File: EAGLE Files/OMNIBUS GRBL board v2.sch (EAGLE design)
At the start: 61 parts, among them K1 691131710002, K2 691131710003, K3 691131710003, K4 691131710003, U1 LTV-847S, U2 L7805ACD2T-TR, U3 LM358M/NOPB, U4 LTV-847S, U5 PC817X3NSZ1B, U6 ULN2003AD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

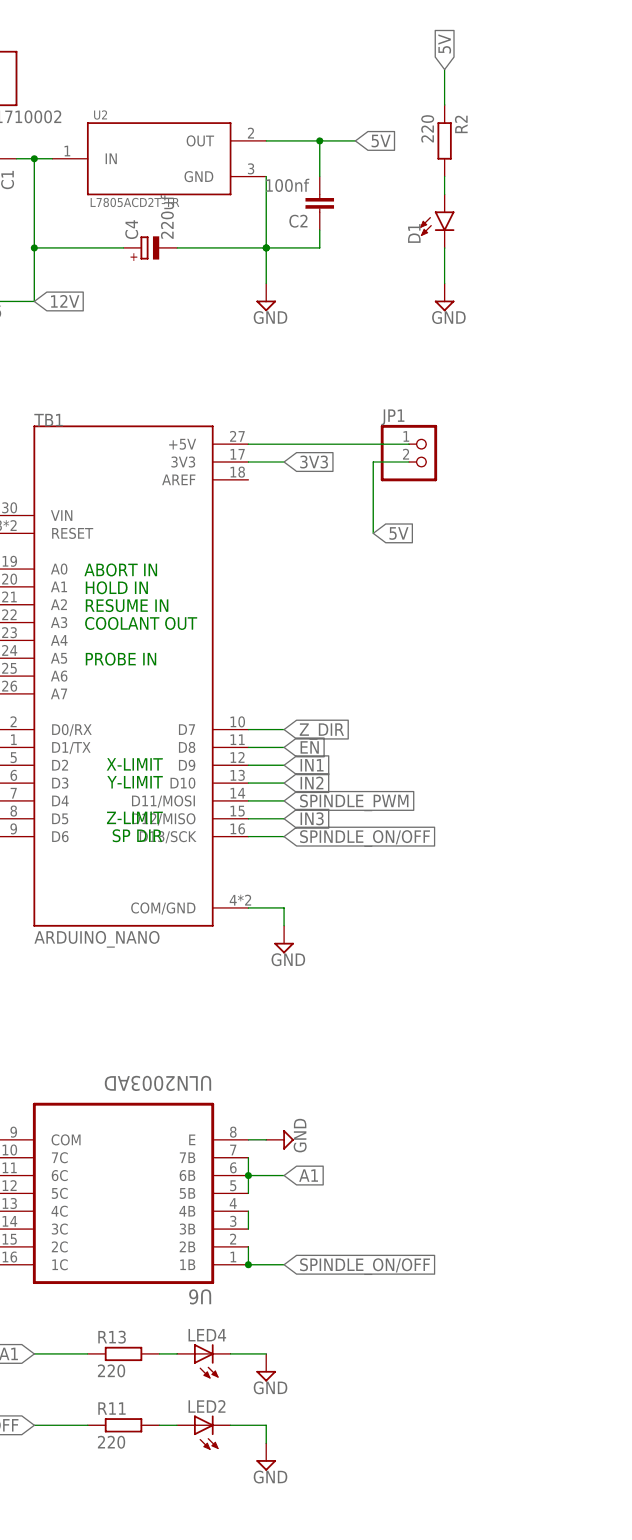
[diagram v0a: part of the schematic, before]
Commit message: PCB Bugfixes and polishing
• DRV Shield had an routing error (laser indicator LED) also R3 had a wrong value
• New Footprint for the 0.33uF Caps
• Silkscreen polishing
• almost all LEDs are 0805 package now
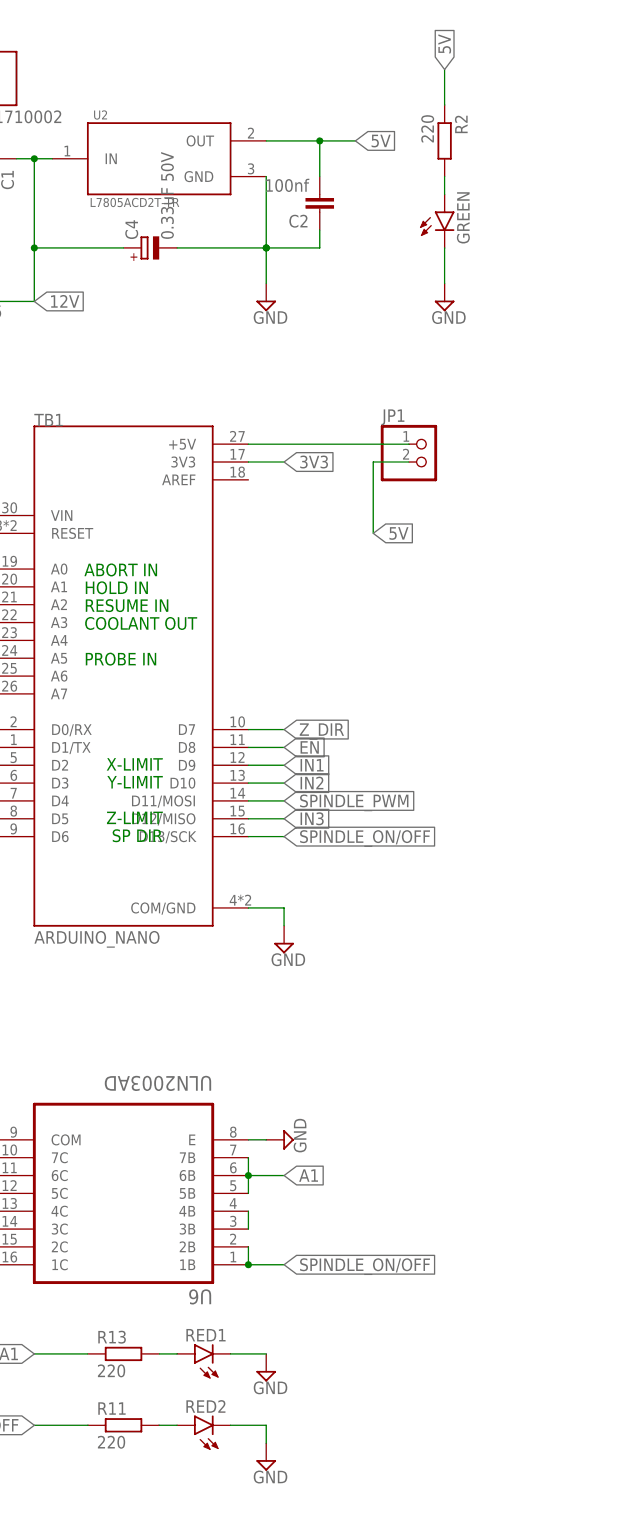
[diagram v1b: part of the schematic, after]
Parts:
- removed D1: (no value), SparkFun-LED:LED1206
- removed LED2, LED4: (no value), eagle-ltspice:LED_ESML0603
- added GREEN, RED1, RED2: (no value), led:LEDCHIPLED_0805
- C4: value 220uf -> 0.33uF 50V; device rcl:CPOL-EUE5-6 -> rcl:CPOL-EUE2-5
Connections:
- net GND: now also GREEN.C, RED1.C, RED2.C; no longer D1.C, LED2.C, LED4.C
- net N$1: now also GREEN.A; no longer D1.A
- net N$11: now also RED2.A; no longer LED2.A
- net N$12: now also RED1.A; no longer LED4.A

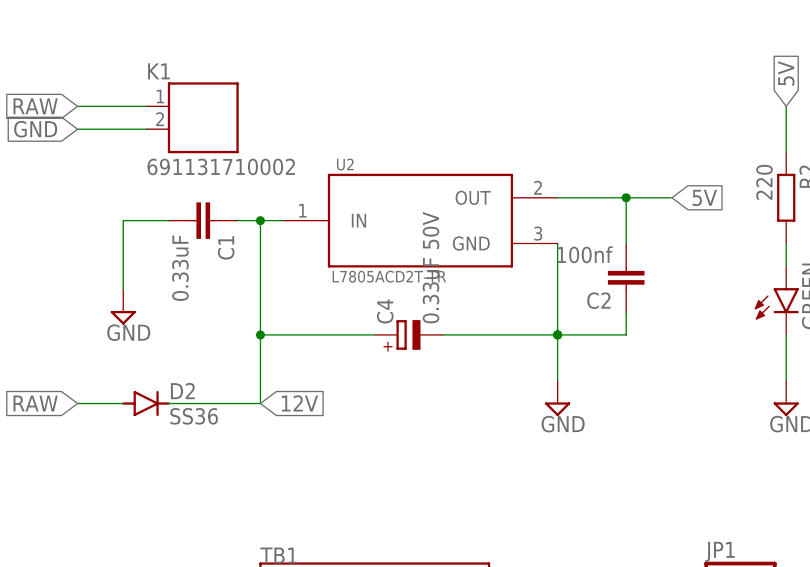
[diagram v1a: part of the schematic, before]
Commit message: Changed voltage regulators
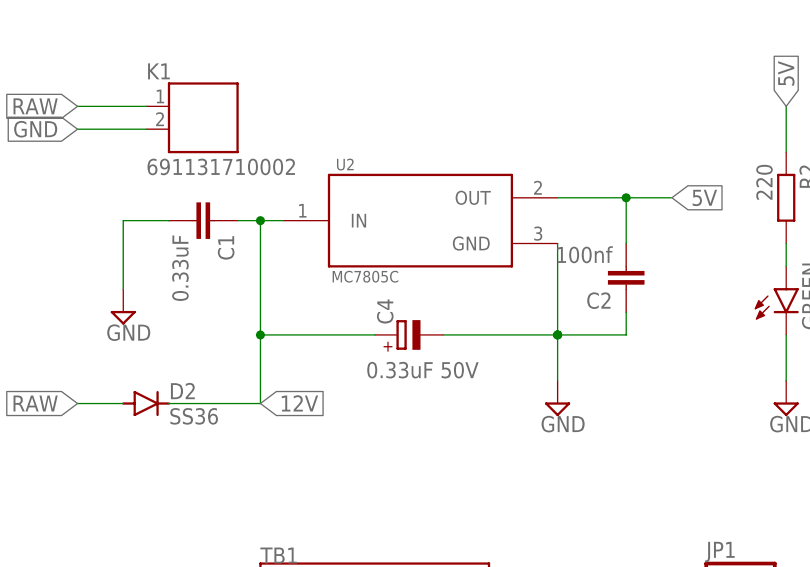
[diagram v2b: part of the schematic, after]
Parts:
- U2: value L7805ACD2T-TR -> MC7805C
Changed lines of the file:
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@@
 <grid distance="0.1" unitdist="inch" unit="inch" style="lines" multiple="1" display="no" altdistance="0.01" altunitdist="inch" altunit="inch"/>
 <layers>
-<layer number="1" name="Top" color="4" fill="1" visible="yes" active="no"/>
-<layer number="2" name="Route2" color="16" fill="1" visible="yes" active="no"/>
-<layer number="3" name="Route3" color="17" fill="1" visible="yes" active="no"/>
-<layer number="4" name="Route4" color="18" fill="1" visible="yes" active="no"/>
-<layer number="5" name="Route5" color="19" fill="1" visible="yes" active="no"/>
-<layer number="6" name="Route6" color="25" fill="1" visible="yes" active="no"/>
-<layer number="7" name="Route7" color="26" fill="1" visible="yes" active="no"/>
-<layer number="8" name="Route8" color="27" fill="1" visible="yes" active="no"/>
-<layer number="9" name="Route9" color="28" fill="1" visible="yes" active="no"/>
-<layer number="10" name="Route10" color="29" fill="1" visible="yes" active="no"/>
-<layer number="11" name="Route11" color="30" fill="1" visible="yes" active="no"/>
-<layer number="12" name="Route12" color="20" fill="1" visible="yes" active="no"/>
-<layer number="13" name="Route13" color="21" fill="1" visible="yes" active="no"/>
-<layer number="14" name="Route14" color="22" fill="1" visible="yes" active="no"/>
-<layer number="15" name="Route15" color="23" fill="1" visible="yes" active="no"/>
-<layer number="16" name="Bottom" color="1" fill="1" visible="yes" active="no"/>
-<layer number="17" name="Pads" color="2" fill="1" visible="yes" active="no"/>
-<layer number="18" name="Vias" color="2" fill="1" visible="yes" active="no"/>
-<layer number="19" name="Unrouted" color="6" fill="1" visible="yes" active="no"/>
-<layer number="20" name="Dimension" color="24" fill="1" visible="yes" active="no"/>
-<layer number="21" name="tPlace" color="7" fill="1" visible="yes" active="no"/>
-<layer number="22" name="bPlace" color="7" fill="1" visible="yes" active="no"/>
-<layer number="23" name="tOrigins" color="15" fill="1" visible="yes" active="no"/>
-<layer number="24" name="bOrigins" color="15" fill="1" visible="yes" active="no"/>
-<layer number="25" name="tNames" color="7" fill="1" visible="yes" active="no"/>
-<layer number="26" name="bNames" color="7" fill="1" visible="yes" active="no"/>
-<layer number="27" name="tValues" color="7" fill="1" visible="yes" active="no"/>
-<layer number="28" name="bValues" color="7" fill="1" visible="yes" active="no"/>
+<layer number="1" name="Top" color="4" fill="1" visible="no" active="no"/>
+<layer number="2" name="Route2" color="16" fill="1" visible="no" active="no"/>
+<layer number="3" name="Route3" color="17" fill="1" visible="no" active="no"/>
+<layer number="4" name="Route4" color="18" fill="1" visible="no" active="no"/>
+<layer number="5" name="Route5" color="19" fill="1" visible="no" active="no"/>
+<layer number="6" name="Route6" color="25" fill="1" visible="no" active="no"/>
+<layer number="7" name="Route7" color="26" fill="1" visible="no" active="no"/>
+<layer number="8" name="Route8" color="27" fill="1" visible="no" active="no"/>
+<layer number="9" name="Route9" color="28" fill="1" visible="no" active="no"/>
+<layer number="10" name="Route10" color="29" fill="1" visible="no" active="no"/>
+<layer number="11" name="Route11" color="30" fill="1" visible="no" active="no"/>
+<layer number="12" name="Route12" color="20" fill="1" visible="no" active="no"/>
+<layer number="13" name="Route13" color="21" fill="1" visible="no" active="no"/>
+<layer number="14" name="Route14" color="22" fill="1" visible="no" active="no"/>
+<layer number="15" name="Route15" color="23" fill="1" visible="no" active="no"/>
+<layer number="16" name="Bottom" color="1" fill="1" visible="no" active="no"/>
+<layer number="17" name="Pads" color="2" fill="1" visible="no" active="no"/>
+<layer number="18" name="Vias" color="2" fill="1" visible="no" active="no"/>
+<layer number="19" name="Unrouted" color="6" fill="1" visible="no" active="no"/>
+<layer number="20" name="Dimension" color="24" fill="1" visible="no" active="no"/>
+<layer number="21" name="tPlace" color="7" fill="1" visible="no" active="no"/>
+<layer number="22" name="bPlace" color="7" fill="1" visible="no" active="no"/>
+<layer number="23" name="tOrigins" color="15" fill="1" visible="no" active="no"/>
+<layer number="24" name="bOrigins" color="15" fill="1" visible="no" active="no"/>
+<layer number="25" name="tNames" color="7" fill="1" visible="no" active="no"/>
+<layer number="26" name="bNames" color="7" fill="1" visible="no" active="no"/>
+<layer number="27" name="tValues" color="7" fill="1" visible="no" active="no"/>
+<layer number="28" name="bValues" color="7" fill="1" visible="no" active="no"/>
 <layer number="29" name="tStop" color="7" fill="3" visible="no" active="no"/>
 <layer number="30" name="bStop" color="7" fill="6" visible="no" active="no"/>
@@
 <layer number="35" name="tGlue" color="7" fill="4" visible="no" active="no"/>
 <layer number="36" name="bGlue" color="7" fill="5" visible="no" active="no"/>
-<layer number="37" name="tTest" color="7" fill="1" visible="yes" active="no"/>
-<layer number="38" name="bTest" color="7" fill="1" visible="yes" active="no"/>
+<layer number="37" name="tTest" color="7" fill="1" visible="no" active="no"/>
+<layer number="38" name="bTest" color="7" fill="1" visible="no" active="no"/>
 <layer number="39" name="tKeepout" color="4" fill="11" visible="no" active="no"/>
 <layer number="40" name="bKeepout" color="1" fill="11" visible="no" active="no"/>
@@
 <layer number="44" name="Drills" color="7" fill="1" visible="no" active="no"/>
 <layer number="45" name="Holes" color="7" fill="1" visible="no" active="no"/>
-<layer number="46" name="Milling" color="3" fill="1" visible="yes" active="no"/>
-<layer number="47" name="Measures" color="7" fill="1" visible="yes" active="no"/>
-<layer number="48" name="Document" color="7" fill="1" visible="yes" active="no"/>
-<layer number="49" name="Reference" color="7" fill="1" visible="yes" active="no"/>
-<layer number="50" name="dxf" color="7" fill="1" visible="yes" active="no"/>
-<layer number="51" name="tDocu" color="7" fill="1" visible="yes" active="no"/>
-<layer number="52" name="bDocu" color="7" fill="1" visible="yes" active="no"/>
-<layer number="53" name="tGND_GNDA" color="7" fill="1" visible="yes" active="no"/>
-<layer number="54" name="bGND_GNDA" color="7" fill="1" visible="yes" active="no"/>
-<layer number="56" name="wert" color="7" fill="1" visible="yes" active="no"/>
-<layer number="57" name="tCAD" color="7" fill="1" visible="yes" active="no"/>
-<layer number="59" name="tCarbon" color="7" fill="1" visible="yes" active="no"/>
-<layer number="60" name="bCarbon" color="7" fill="1" visible="yes" active="no"/>
+<layer number="46" name="Milling" color="3" fill="1" visible="no" active="no"/>
+<layer number="47" name="Measures" color="7" fill="1" visible="no" active="no"/>
+<layer number="48" name="Document" color="7" fill="1" visible="no" active="no"/>
+<layer number="49" name="Reference" color="7" fill="1" visible="no" active="no"/>
+<layer number="50" name="dxf" color="7" fill="1" visible="no" active="no"/>
+<layer number="51" name="tDocu" color="7" fill="1" visible="no" active="no"/>
+<layer number="52" name="bDocu" color="7" fill="1" visible="no" active="no"/>
+<layer number="53" name="tGND_GNDA" color="7" fill="1" visible="no" active="no"/>
+<layer number="54" name="bGND_GNDA" color="7" fill="1" visible="no" active="no"/>
+<layer number="56" name="wert" color="7" fill="1" visible="no" active="no"/>
+<layer number="57" name="tCAD" color="7" fill="1" visible="no" active="no"/>
+<layer number="59" name="tCarbon" color="7" fill="1" visible="no" active="no"/>
+<layer number="60" name="bCarbon" color="7" fill="1" visible="no" active="no"/>
 <layer number="88" name="SimResults" color="9" fill="1" visible="yes" active="yes"/>
 <layer number="89" name="SimProbes" color="9" fill="1" visible="yes" active="yes"/>
@@
 <part name="K1" library="Wurth_Terminal_Blocks_Connectors_rev15d" deviceset="691131710002" device=""/>
 <part name="U1" library="LTV-847S" deviceset="LTV-847S" device=""/>
-<part name="U2" library="L7805ACD2T-TR" deviceset="L7805ACD2T-TR" device=""/>
+<part name="U2" library="L7805ACD2T-TR" deviceset="L7805ACD2T-TR" device="" value="MC7805C"/>
 <part name="U3" library="LM358M_NOPB" deviceset="LM358M/NOPB" device=""/>
 <part name="VR1" library="3296W-1-502" deviceset="3296W-1-502" device="" value="10k"/>
@@
 <instance part="C4" gate="G$1" x="33.02" y="175.26" smashed="yes" rot="R90">
 <attribute name="NAME" x="32.5374" y="176.403" size="1.778" layer="95" rot="R90"/>
-<attribute name="VALUE" x="37.6174" y="176.403" size="1.778" layer="96" rot="R90"/>
+<attribute name="VALUE" x="42.037" y="172.2374" size="1.778" layer="96" rot="R180"/>
 </instance>
 <instance part="RESET" gate="-1" x="170.18" y="43.18" smashed="yes" rot="R90">

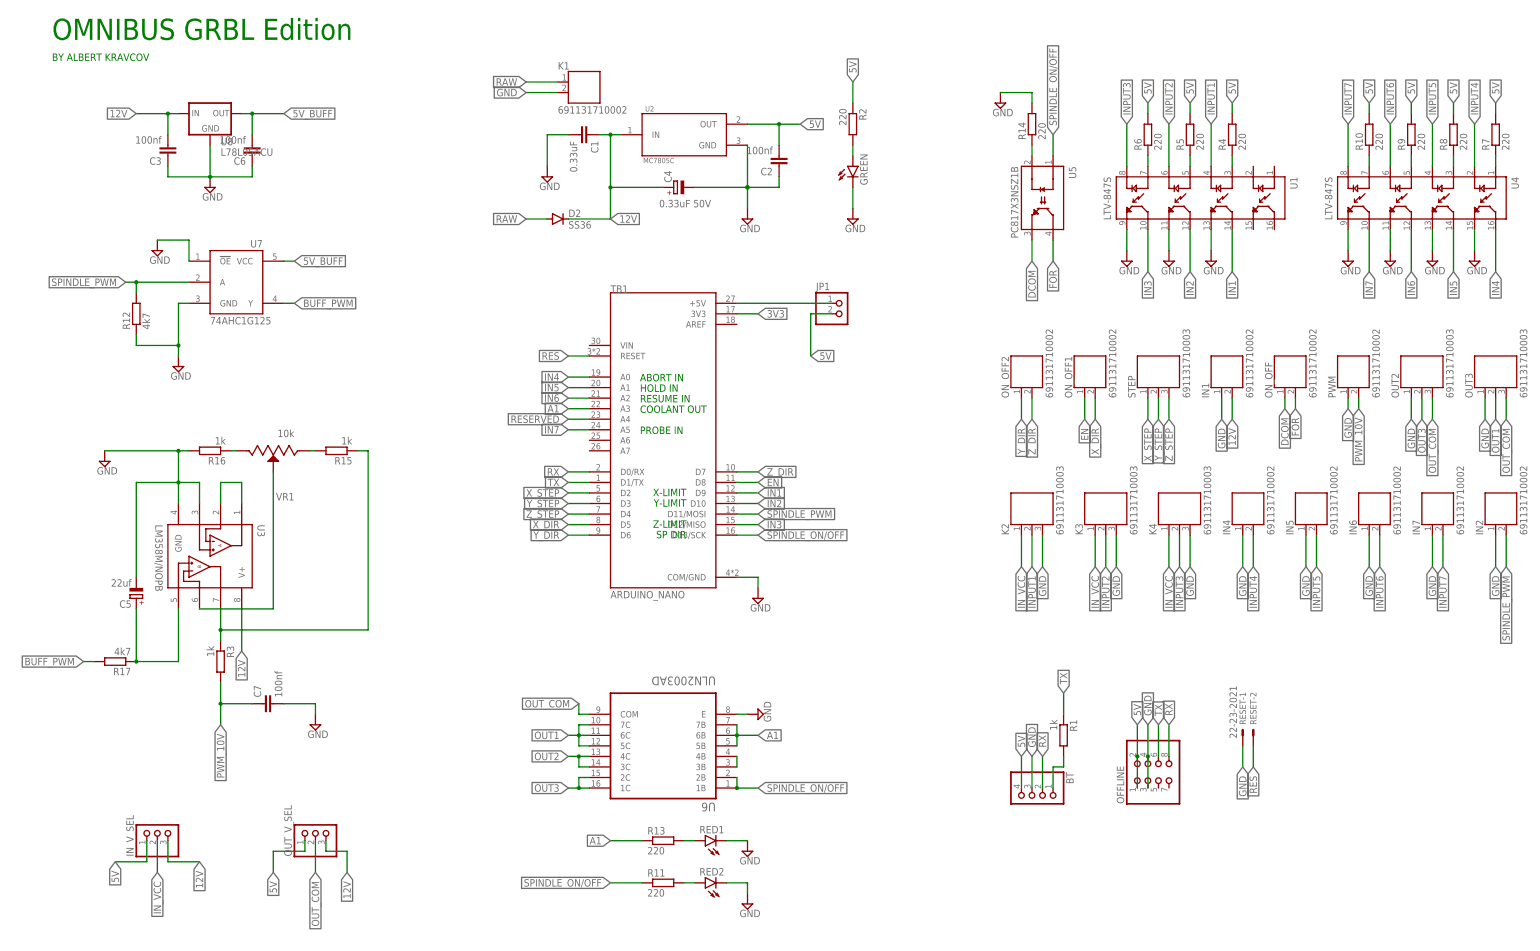
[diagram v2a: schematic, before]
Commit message: clean up
also added BOM
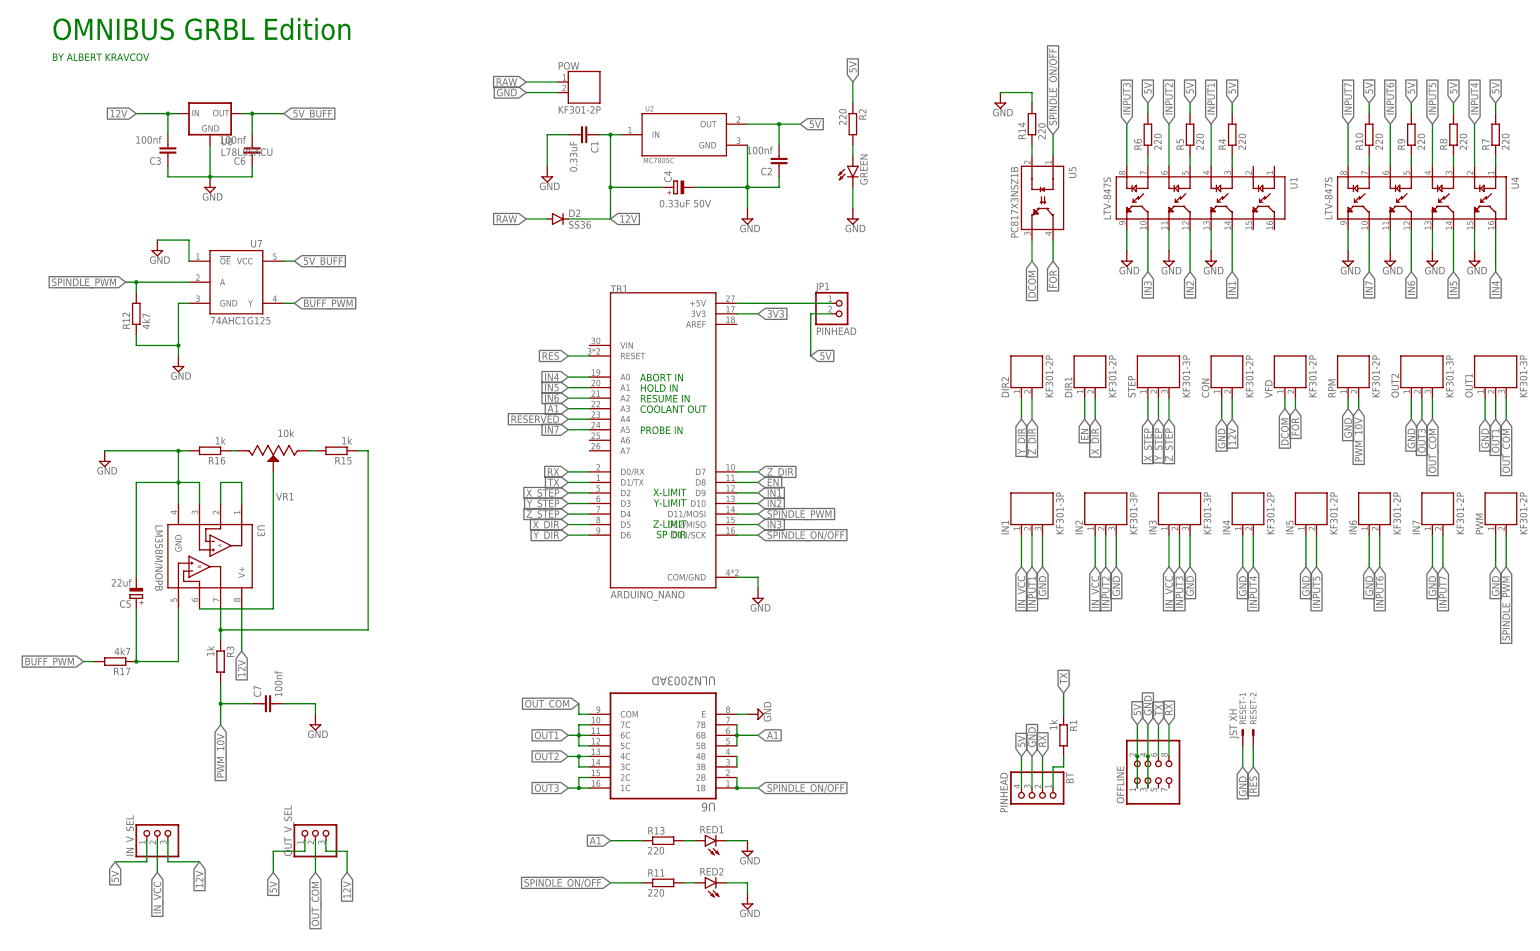
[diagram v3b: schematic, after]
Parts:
- removed K2, K3: 691131710003, Wurth_Terminal_Blocks_Connectors_rev15d:691131710003
- added CON, RPM: KF301-2P, Wurth_Terminal_Blocks_Connectors_rev15d:691131710002
- BT, JP1: value (none) -> PINHEAD
- DIR1, DIR2, IN4, IN5, IN6, IN7, POW, PWM, VFD: value 691131710002 -> KF301-2P
- IN1, IN2: value 691131710002 -> KF301-3P; device Wurth_Terminal_Blocks_Connectors_rev15d:691131710002 -> Wurth_Terminal_Blocks_Connectors_rev15d:691131710003
- IN3, OUT1, OUT2, STEP: value 691131710003 -> KF301-3P
- RESET: value 22-23-2021 -> JST XH
- renumbered K1 to POW, K4 to IN3, ON_OFF to VFD, ON_OFF1 to DIR1, ON_OFF2 to DIR2, OUT3 to OUT1
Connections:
- net 12V: now also CON.2; no longer IN1.2
- net GND: now also CON.1, IN1.3, IN2.3, RPM.1; no longer IN1.1, IN2.1, K2.3, K3.3
- net INPUT1: now also IN1.2; no longer K2.2
- net INPUT2: now also IN2.2; no longer K3.2
- net IN_VCC: now also IN1.1, IN2.1; no longer K2.1, K3.1
- net PWM_10V: now also RPM.2; no longer PWM.2
- net SPINDLE_PWM: now also PWM.2; no longer IN2.2
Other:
- moved on the sheet: PWM
